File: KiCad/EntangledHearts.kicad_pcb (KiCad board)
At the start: 2 copper layers, 17 parts

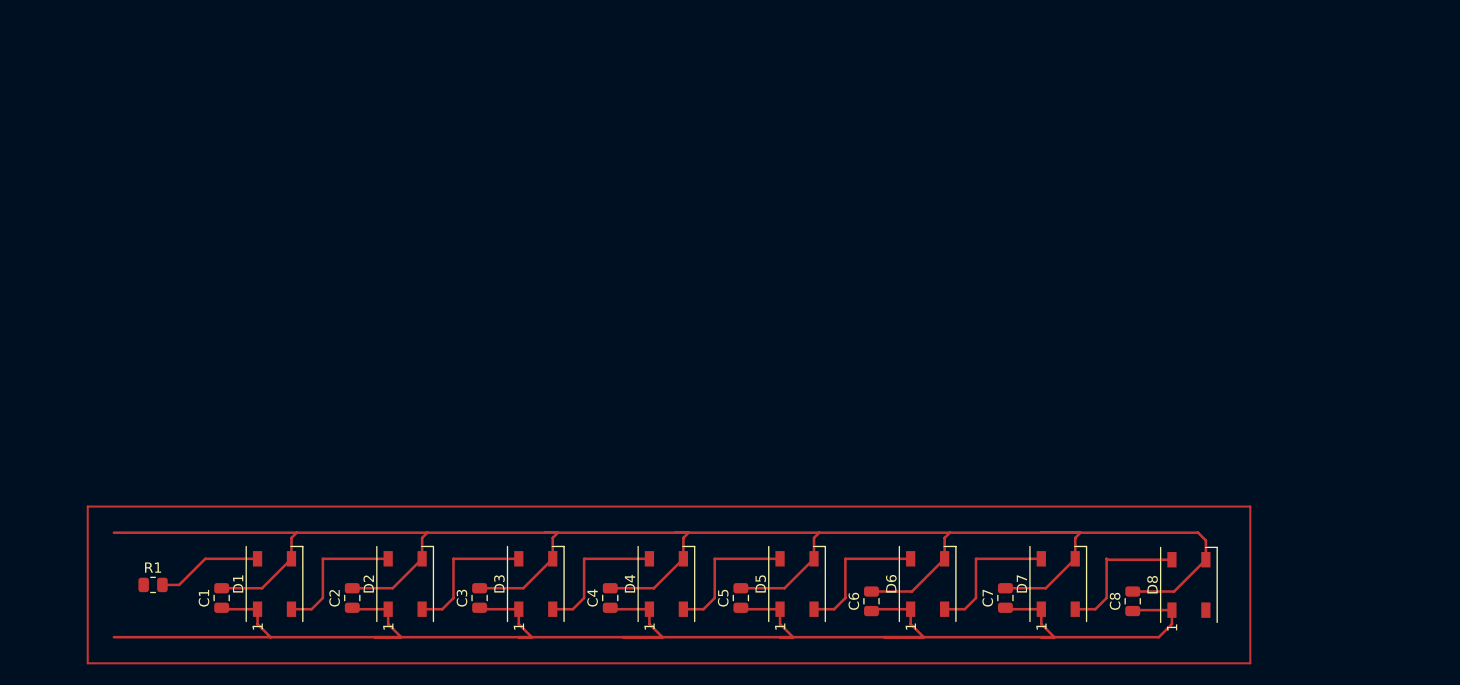
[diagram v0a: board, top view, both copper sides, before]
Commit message: ADD: PCB for NeoPixels started
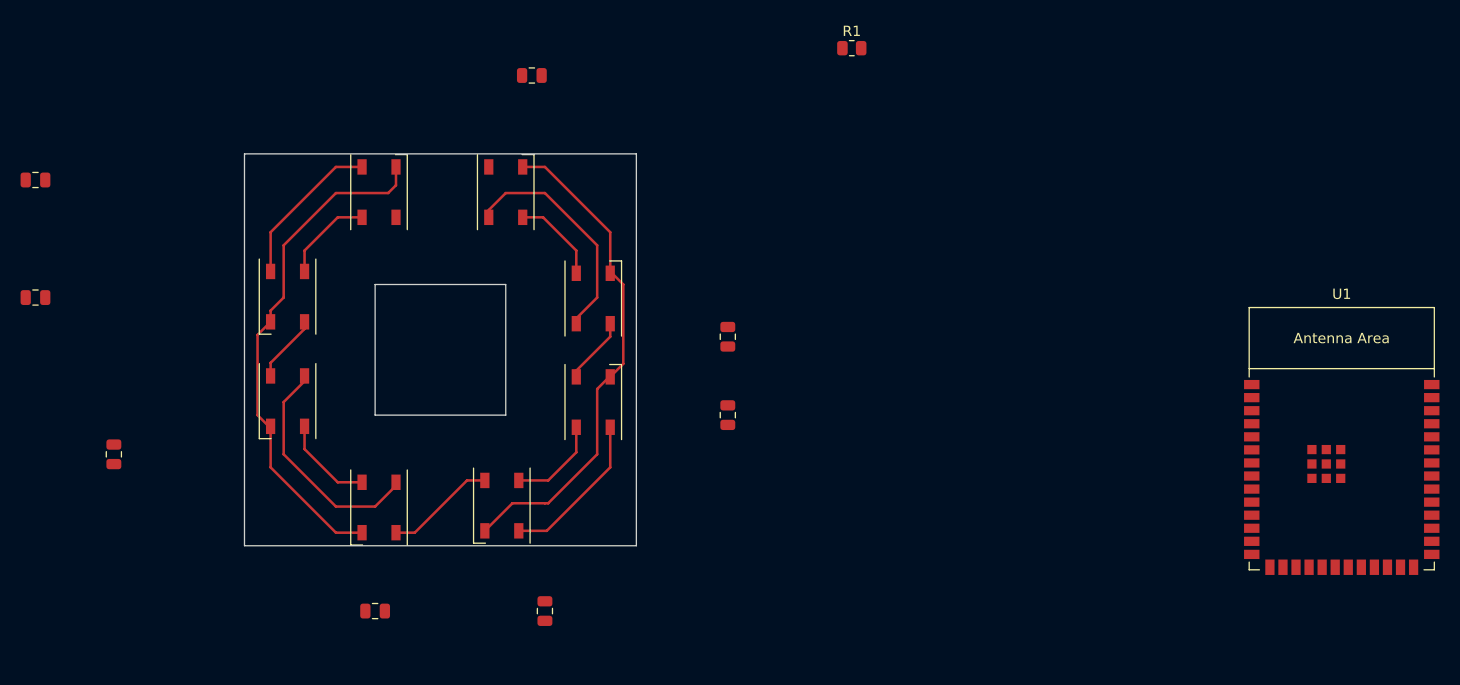
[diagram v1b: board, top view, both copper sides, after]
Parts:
- added U1: ESP32-S3-WROOM-1, PCM_Espressif:ESP32-S3-WROOM-1, F.Cu at (208.3, 81.5)
- moved C8 110.7 mm to (81.3, 64.8), turned to 0 degrees
- moved C7 102.7 mm to (81.3, 53.3), turned to 180 degrees
- moved D8 87.5 mm to (114.7, 54.5)
- moved R1 85.7 mm to (160.6, 40.5)
- moved D7 80.0 mm to (105.8, 64.7), turned to -90 degrees
- moved C6 75.0 mm to (88.9, 80.0), turned to -90 degrees
- moved D6 64.7 mm to (105.8, 74.8), turned to -90 degrees
- moved C1 59.1 mm to (129.5, 43.2), turned to 0 degrees
- moved C2 44.5 mm to (148.6, 68.6), turned to -90 degrees
- moved D1 44.2 mm to (127.0, 54.5)
- moved D5 41.3 mm to (114.7, 85.2), turned to -90 degrees
- moved C5 35.6 mm to (114.3, 95.2), turned to 180 degrees
- moved D2 33.2 mm to (135.5, 64.9)
- moved C3 30.0 mm to (148.6, 76.2)
- moved D3 18.6 mm to (135.5, 74.9)
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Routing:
- net +3.3V: track 171.4 -> 64.9 mm
- net GND: track 199.6 -> 98.8 mm
- net Net-(D1-DIN): track 10.3 -> 0.00 mm
- net Net-(D2-DOUT): track 13.7 -> 6.54 mm
- net Net-(D6-DOUT): track 13.7 -> 6.63 mm
- net Net-(D1-DOUT): track 13.7 -> 8.76 mm
- net Net-(D5-DOUT): track 13.7 -> 9.14 mm
- net Net-(D4-DOUT): track 13.7 -> 10.7 mm
- net Net-(D3-DOUT): track 13.7 -> 15.3 mm
- net Net-(D7-DOUT): track 13.7 -> 15.3 mm
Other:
- board outline added: 38.1 x 38.1 mm
